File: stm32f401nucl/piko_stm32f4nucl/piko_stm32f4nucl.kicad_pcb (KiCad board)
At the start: 2 copper layers, 3 parts, among them U1 NUCLEO-64

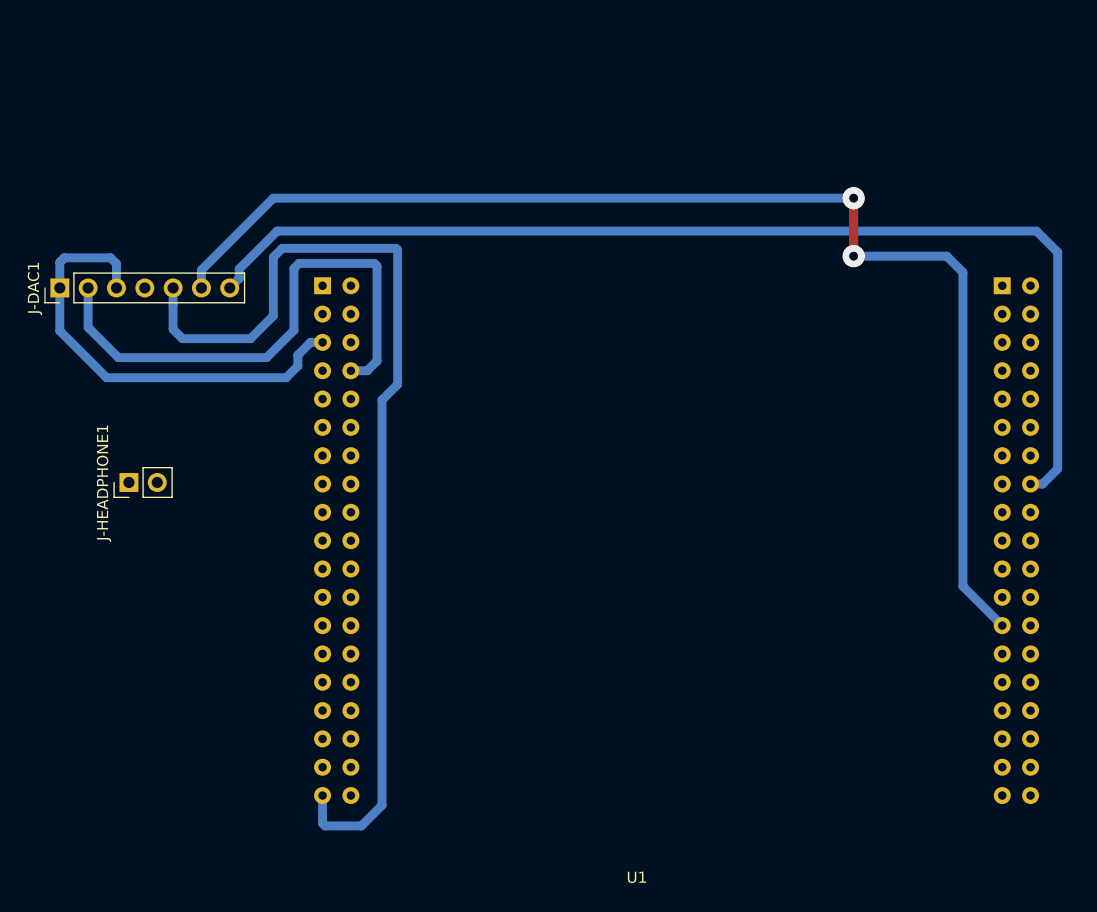
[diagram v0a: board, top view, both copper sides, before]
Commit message: pcb design for stm32f401nucl
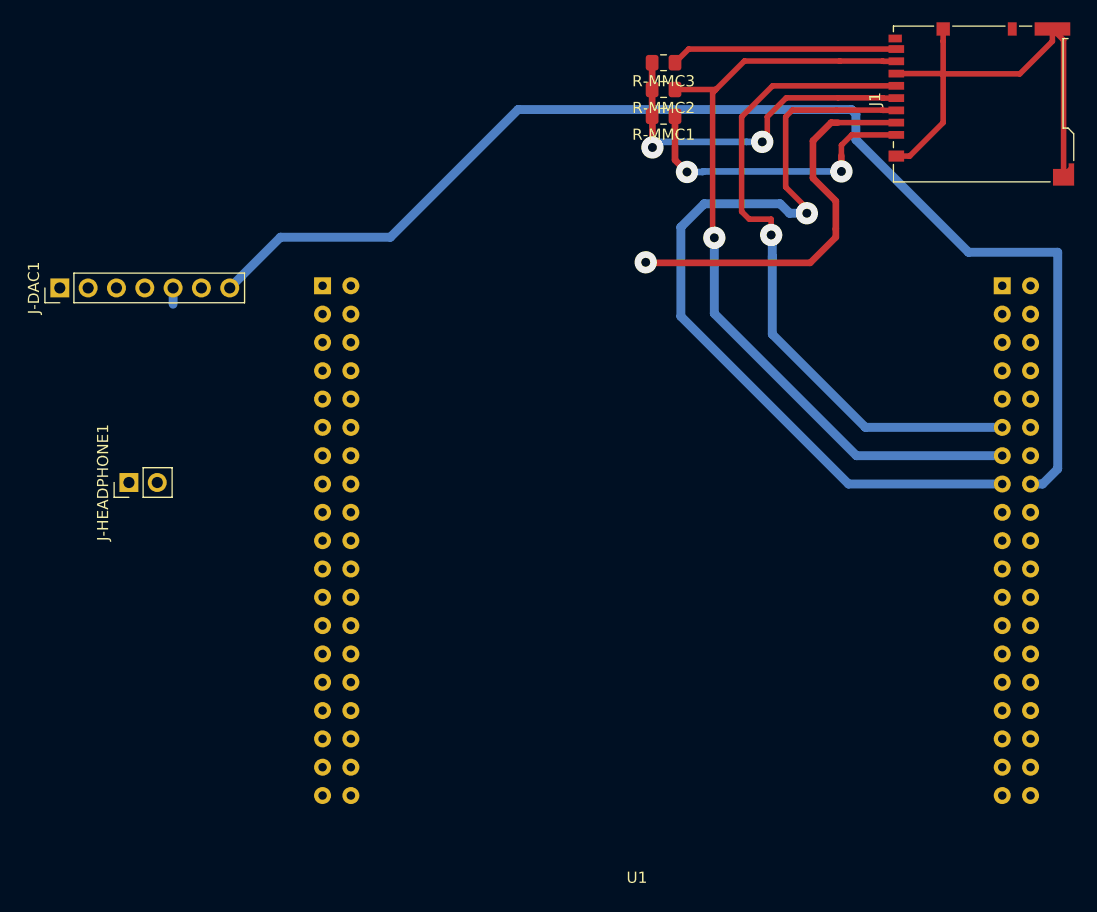
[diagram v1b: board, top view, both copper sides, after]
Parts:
- added J1: Micro_SD_Card_Det, Connector_Card:microSD_HC_Hirose_DM3BT-DSF-PEJS, F.Cu at (182.9, 65.8)
- added R-MMC1: 10k, Resistor_SMD:R_0805_2012Metric_Pad1.15x1.40mm_HandSolder, F.Cu at (154.4, 67.0)
- added R-MMC2: 10k, Resistor_SMD:R_0805_2012Metric_Pad1.15x1.40mm_HandSolder, F.Cu at (154.4, 64.5)
- added R-MMC3: 10k, Resistor_SMD:R_0805_2012Metric_Pad1.15x1.40mm_HandSolder, F.Cu at (154.4, 62.1)
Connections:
- U1 pad 32: Net-(U1-Pad32) -> /MMC_NSS
- U1 pad 49: Net-(U1-Pad49) -> /MMC_SCK
- U1 pad 51: Net-(U1-Pad51) -> /MMC_MISO
- U1 pad 53: Net-(U1-Pad53) -> /MMC_MOSI
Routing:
- net /BCLK: track 111.5 -> 0.00 mm, vias 2 -> 0
- net /DATA: track 89.8 -> 1.46 mm
- net /MMC_MOSI: track 0.00 -> 75.4 mm, vias 0 -> 1
- net /MMC_MISO: track 0.00 -> 72.3 mm, vias 0 -> 1
- net /MMC_SCK: track 0.00 -> 61.5 mm, vias 0 -> 1
- net /MMC_NSS: track 0.00 -> 35.7 mm, vias 0 -> 1
- net Net-(J1-Pad1): track 0.00 -> 27.0 mm, vias 0 -> 2
- net Net-(J1-Pad8): track 0.00 -> 20.4 mm
- net /LRC: track 100.1 -> 110.0 mm
- net VDD: track 41.0 -> 32.4 mm, vias 0 -> 2
- net GND: track 48.6 -> 43.9 mm
